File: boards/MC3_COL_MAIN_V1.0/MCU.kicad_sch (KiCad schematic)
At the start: 30 parts, among them J2 SWD, SW1 SKRKAEE020, U2 STM32F412RET6, Y1 8MHz

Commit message: Vault: COL-COTS-0029 for the STM32F412RET6, with DS11139 filed
Created in the design wiki (not this repo - the vault is the authority):
- Datasheets/PDFs/STM32F412xE-xG.pdf, byte-identical copy of the download
  (md5 15412db4b9fff30cc7b071fd2c746927), plus the REF note
  "ST STM32F412xE-xG datasheet" pointing at it.
- 04 Records/COTS/COL-COTS-0029.md. Reasoning: the machine control link was
  specified as CAN and the F411 has no CAN controller, so the alternative was an
  external SPI-to-CAN part. The F412 is pin-identical - same LQFP64, pin map, AF
  map and decoupling - so only two nets moved, and it brings 256 KB RAM. G4 was
  not re-surveyed; COL-SEARCH-0008 already rejected it on cost and stock and
  adding CAN does not change that.
- COL-COTS-0024 marked superseded_by 0029 with a note at the top; the datasheet
  index now lists the F412 as the fitted part and keeps the F411 row for trail.

The cover page also settles the earlier open question: "Up to 4x I2C interfaces"
and "2x CAN (2.0B Active)". MIGRATION section 9 updated from unverified to
verified, and the records-owed list marks the MCU record done.

Repo side now cites the real ID: U2's COTS field in MCU.kicad_sch, and
docs/design/parts/STM32F412.md and its README.

Co-Authored-By: Claude Opus 5 (1M context) <noreply@anthropic.com>
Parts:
- U2: COTS COL-COTS-TBD (new record: supersedes COL-COTS-0024 STM32F41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 -> COL-COTS-0029 (STM32F412RET6; supersedes COL-COTS-0024 STM3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
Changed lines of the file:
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@@
 			)
 		)
-		(property "COTS" "COL-COTS-TBD (new record: supersedes COL-COTS-0024 STM32F411RET6 - pin-identical sibling with bxCAN x2 and 256 KB RAM)"
+		(property "COTS" "COL-COTS-0029 (STM32F412RET6; supersedes COL-COTS-0024 STM32F411RET6 - pin-identical sibling with bxCAN)"
 			(at 149.86 100.33 0)
 			(hide yes)

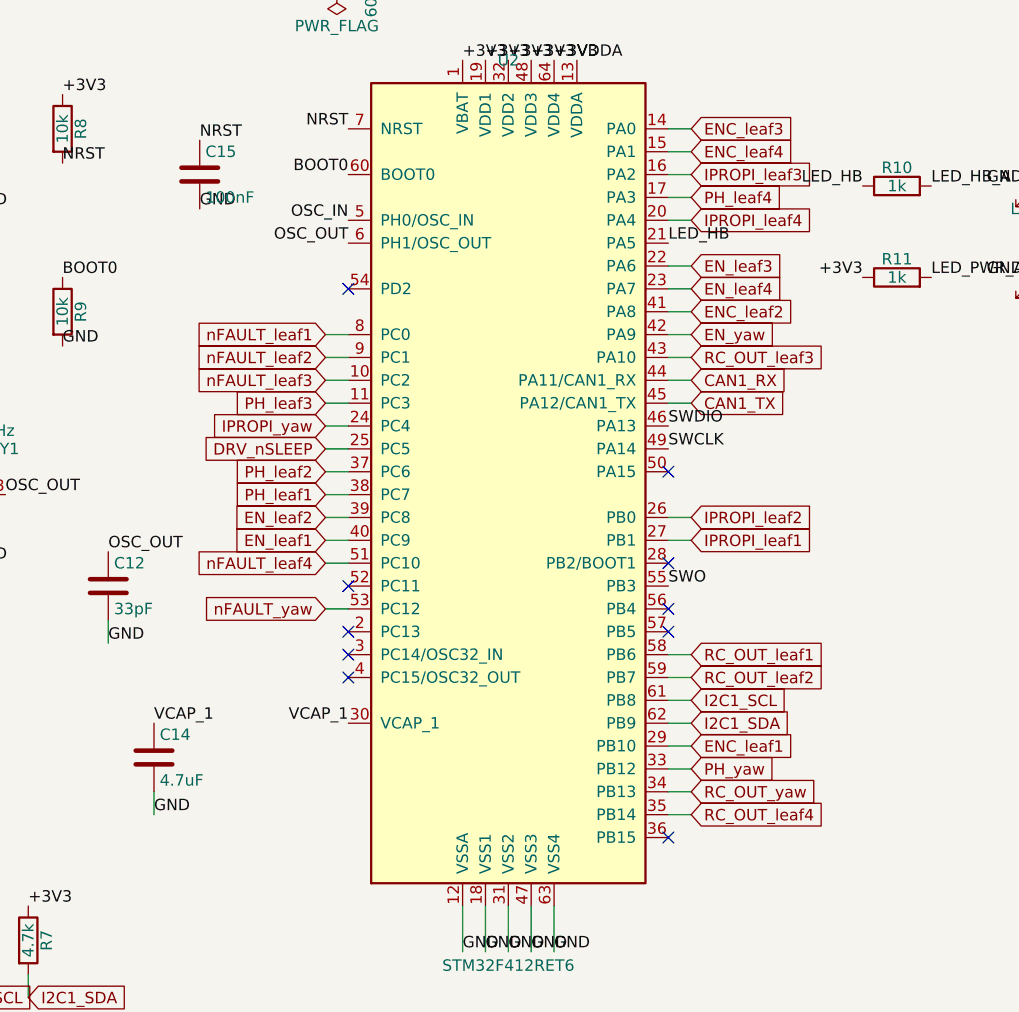
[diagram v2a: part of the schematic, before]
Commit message: MCU pin remap: channels grouped by edge (S=leaf3/4, E=leaf4-tail/leaf1/leaf2, N=leaf2-tail/yaw, W=leaf3/4 spare)
All 4 leaf EN stay on TIM3 (CH1 leaf4, CH2 leaf3, CH3 leaf1, CH4 leaf2), yaw EN on TIM1_CH2.
All 5 RC_OUT now on timer-capture pins (TIM5/TIM12/TIM1/TIM4). All 4 ENC on TIM2/TIM5 capture.
All 5 IPROPI on ADC pins. ERC 0 errors.

Co-Authored-By: Claude Fable 5 <noreply@anthropic.com>
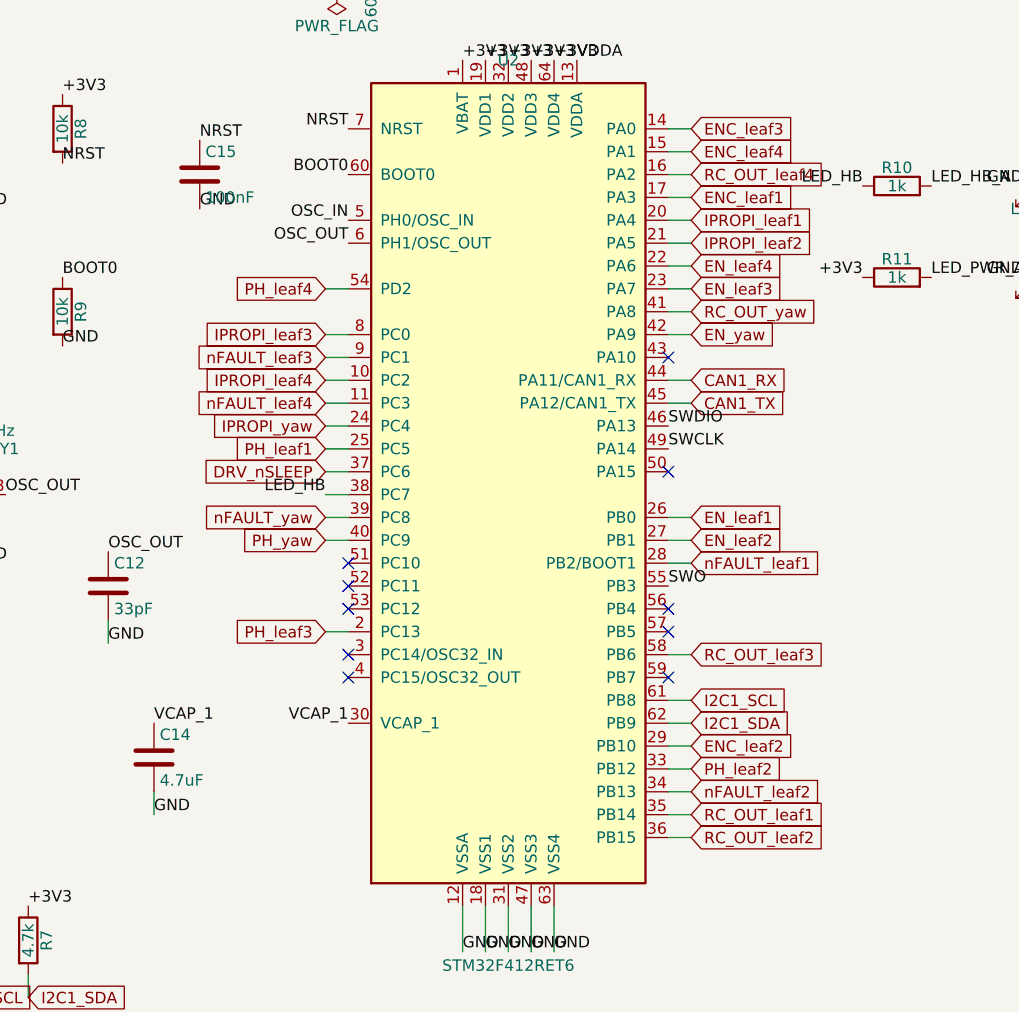
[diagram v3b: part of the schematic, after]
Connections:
- net DRV_nSLEEP: now also U2.37 (PC6); no longer U2.25 (PC5)
- net ENC_leaf1: now also U2.17 (PA3); no longer U2.29 (PB10)
- net ENC_leaf2: now also U2.29 (PB10); no longer U2.41 (PA8)
- net EN_leaf1: now also U2.26 (PB0); no longer U2.40 (PC9)
- net EN_leaf2: now also U2.27 (PB1); no longer U2.39 (PC8)
- net EN_leaf3: now also U2.23 (PA7); no longer U2.22 (PA6)
- net EN_leaf4: now also U2.22 (PA6); no longer U2.23 (PA7)
- net IPROPI_leaf1: now also U2.20 (PA4); no longer U2.27 (PB1)
- net IPROPI_leaf2: now also U2.21 (PA5); no longer U2.26 (PB0)
- net IPROPI_leaf3: now also U2.8 (PC0); no longer U2.16 (PA2)
- net IPROPI_leaf4: now also U2.10 (PC2); no longer U2.20 (PA4)
- net LED_HB: now also U2.38 (PC7); no longer U2.21 (PA5)
- net PH_leaf1: now also U2.25 (PC5); no longer U2.38 (PC7)
- net PH_leaf2: now also U2.33 (PB12); no longer U2.37 (PC6)
- net PH_leaf3: now also U2.2 (PC13); no longer U2.11 (PC3)
- net PH_leaf4: now also U2.54 (PD2); no longer U2.17 (PA3)
- net PH_yaw: now also U2.40 (PC9); no longer U2.33 (PB12)
- net RC_OUT_leaf1: now also U2.35 (PB14); no longer U2.58 (PB6)
- net RC_OUT_leaf2: now also U2.36 (PB15); no longer U2.59 (PB7)
- net RC_OUT_leaf3: now also U2.58 (PB6); no longer U2.43 (PA10)
- net RC_OUT_leaf4: now also U2.16 (PA2); no longer U2.35 (PB14)
- net RC_OUT_yaw: now also U2.41 (PA8); no longer U2.34 (PB13)
- net nFAULT_leaf1: now also U2.28 (PB2/BOOT1); no longer U2.8 (PC0)
- net nFAULT_leaf2: now also U2.34 (PB13); no longer U2.9 (PC1)
- net nFAULT_leaf3: now also U2.9 (PC1); no longer U2.10 (PC2)
- net nFAULT_leaf4: now also U2.11 (PC3); no longer U2.51 (PC10)
- net nFAULT_yaw: now also U2.39 (PC8); no longer U2.53 (PC12)

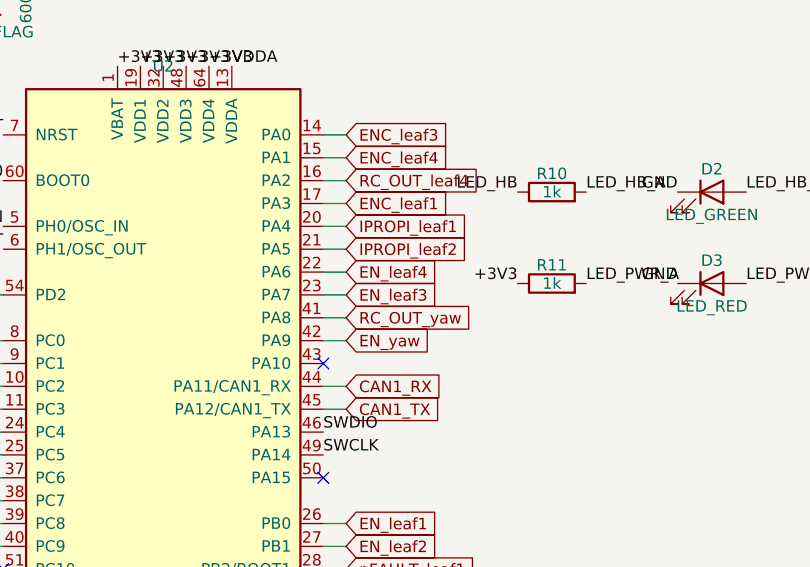
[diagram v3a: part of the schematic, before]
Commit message: Swap EN_leaf3/EN_leaf4: PA6=EN_leaf3 (TIM3_CH1), PA7=EN_leaf4 (TIM3_CH2)
Co-Authored-By: Claude Fable 5 <noreply@anthropic.com>
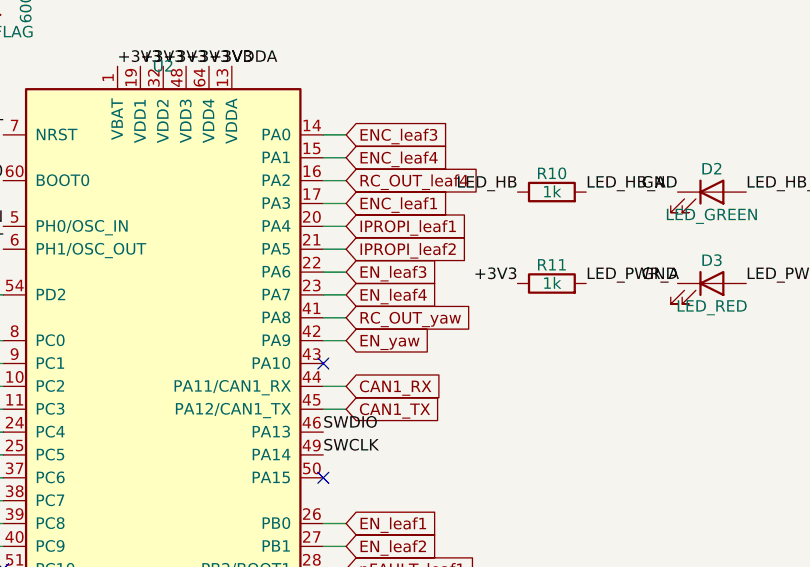
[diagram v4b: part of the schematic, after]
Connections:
- net EN_leaf3: now also U2.22 (PA6); no longer U2.23 (PA7)
- net EN_leaf4: now also U2.23 (PA7); no longer U2.22 (PA6)
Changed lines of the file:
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@@
-		)
-	)
-	(global_label "EN_leaf4"
-		(shape input)
-		(at 170.18 74.93 0)
-		(effects
-			(font
-				(size 1.27 1.27)
-			)
-			(justify left)
-		)
-	)
-	(global_label "EN_leaf3"
-		(shape input)
-		(at 170.18 77.47 0)
-		(effects
-			(font
-				(size 1.27 1.27)
-			)
-			(justify left)
 		)
 	)
@@
 		(effects
 			(font
+				(size 1.27 1.27)
+			)
+			(justify left)
+		)
+	)
+	(global_label "EN_leaf3"
+		(shape input)
+		(at 170.18 74.93 0)
+		(effects
+			(font
+				(size 1.27 1.27)
+			)
+			(justify left)
+		)
+	)
+	(global_label "EN_leaf4"
+		(shape input)
+		(at 170.18 77.47 0)
+		(effects
+			(font

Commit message: Yaw encoder: AEDR-8300 (U9, C22453800) on TIM2 PA15/PB3; SWO dropped for RTT; debug UART PC10/PC11 (J2 old SWO pin = DBG_TX, TP8 = DBG_RX); VSENS promoted to global net
Co-Authored-By: Claude Fable 5 <noreply@anthropic.com>
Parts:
- added C33: 100nF, MC3_COL_MAIN:C_0402_1005Metric, symbol Device:C
- added R33: 220R, MC3_COL_MAIN:R_0402_1005Metric, symbol Device:R
- added R34, R35: 2.2k, MC3_COL_MAIN:R_0402_1005Metric, symbol Device:R
- added TP8: DBG_RX, MC3_COL_MAIN:TestPoint_Pad_1.0x1.0mm, symbol Connector:TestPoint
- added U9: AEDR-8300-1Q0, MC3_COL_MAIN:AEDR-8300, symbol MC3_COL_MAIN:AEDR-8300
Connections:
- net +3V3: now also R34.1, R35.1
- net GND: now also C33.2, U9.2 (GND), U9.4 (GND)
- net YAW_ENC_A: now reaches U2.50 (PA15)
- net YAW_ENC_A: now also R34.2, U9.5 (CHA)
- net DBG_TX: now reaches U2.51 (PC10)
- net DBG_TX: now also J2.6 (Pin_6)
- net DBG_RX: now reaches U2.52 (PC11)
- net DBG_RX: now also TP8.1
- net SWO renamed YAW_ENC_B
- net YAW_ENC_B: now also R35.2, U9.1 (CHB); no longer J2.6 (Pin_6)
- new net: R33.2, U9.3 (VLED)
- new net VSENS: C33.1, R33.1, U9.6 (VCC)
- no-connect marks 10 -> 7

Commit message: Yaw homing datum: GP1S092HCPIF interrupter (U10, C69422, PROVISIONAL) on PB7/TIM4_CH2; footprint+pin numbers owed until Sharp datasheet lands
Co-Authored-By: Claude Fable 5 <noreply@anthropic.com>
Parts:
- added R36: 220R, MC3_COL_MAIN:R_0402_1005Metric, symbol Device:R
- added R37: 10k, MC3_COL_MAIN:R_0402_1005Metric, symbol Device:R
- added U10: GP1S092HCPIF, symbol MC3_COL_MAIN:GP1S092HCPIF
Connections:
- net +3V3: now also R36.1, R37.1
- net GND: now also U10.2 (K), U10.4 (E)
- net YAW_HOME: now reaches U2.59 (PB7)
- net YAW_HOME: now also R37.2, U10.3 (C)
- new net: R36.2, U10.1 (A)
- no-connect marks 7 -> 6

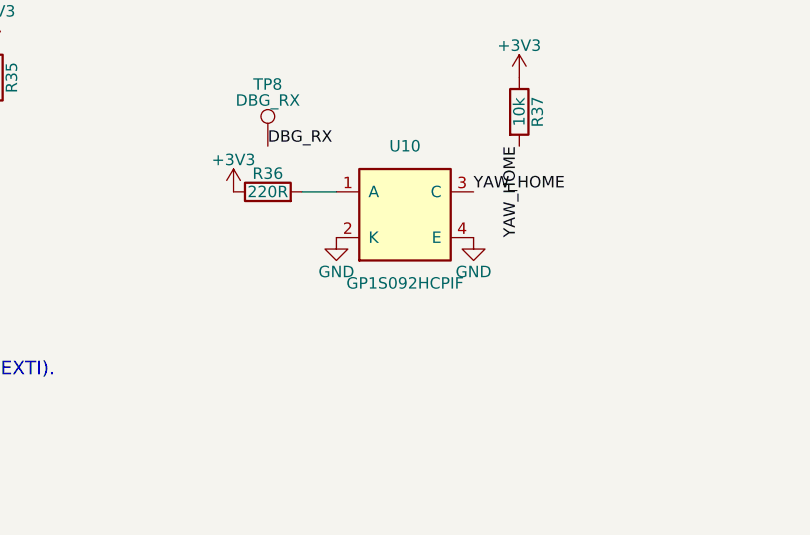
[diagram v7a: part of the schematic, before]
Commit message: Homing interrupter -> GP1S094HCZ0F (C920601, 3mm slot, user decision); COL-COTS-0034, 0033 rejected
Co-Authored-By: Claude Fable 5 <noreply@anthropic.com>
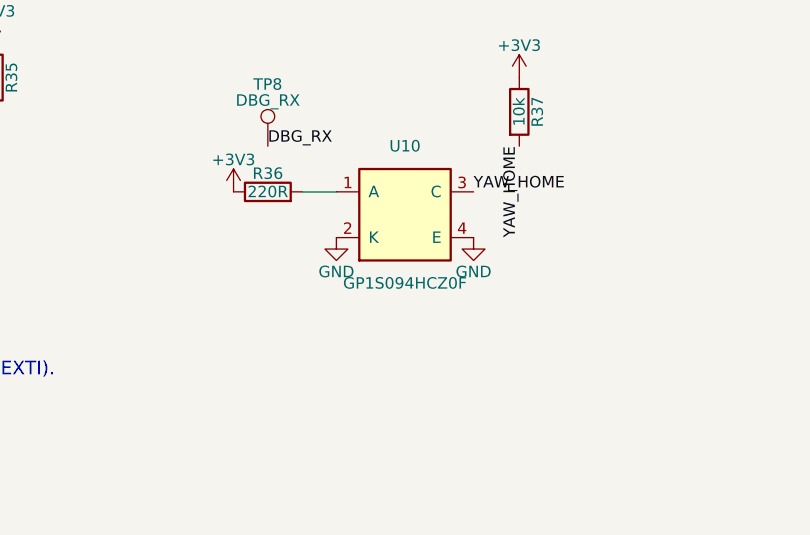
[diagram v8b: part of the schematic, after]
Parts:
- removed U10: GP1S092HCPIF, symbol MC3_COL_MAIN:GP1S092HCPIF
- added U10: GP1S094HCZ0F, symbol MC3_COL_MAIN:GP1S094HCZ0F
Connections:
- net GND: now also U10.2 (K), U10.4 (E)
- net YAW_HOME: now also U10.3 (C)
- net at R36.2: now also U10.1 (A)
